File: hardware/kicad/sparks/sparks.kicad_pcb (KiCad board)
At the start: 2 copper layers, 39 parts, among them J1 Conn_02x04_Odd_Even, J2 TP4056 Breakout, SW1 SW_Push, U1 MAX7219, U2 ESP32-C3-SuperMini

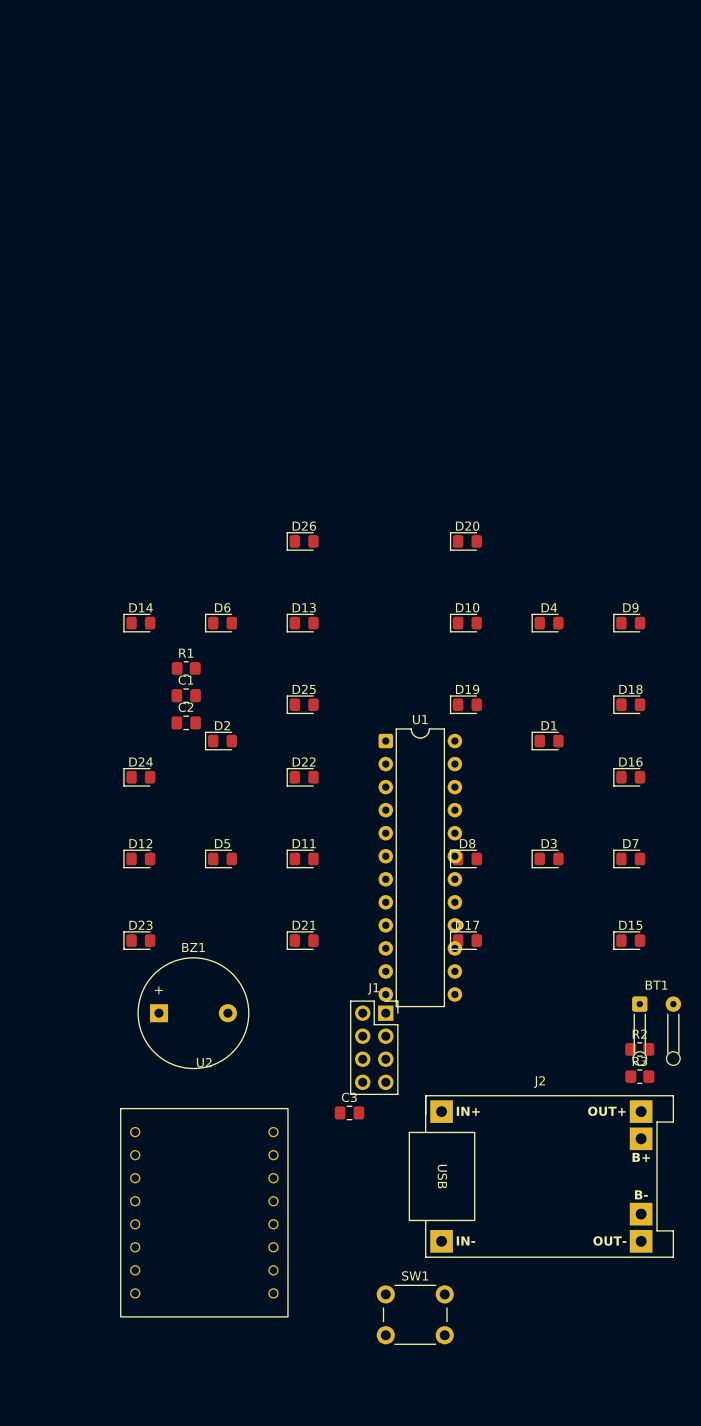
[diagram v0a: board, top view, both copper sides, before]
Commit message: Correct the panel to a 7x7 grid
The previous placement generated an extra empty column, because X
sat on an odd half-step while every other letter fell on a whole
one. The panel is a 7x7 grid with 26 of the 49 cells filled:

    O M T E I S H
    Q G - - U V -
    - Z - - F - -
    Y K N A R L -
    - C - - - - -
    - X D W P - -
    - - B J - - -

Row 0 is the repeated-symbol spine, reading H S I E outward to the
right and T M O to the left. Row 3 is the second spine, where the
code switches symbol once: A R L rightward, N K Y leftward.
Everything else hangs off those two rows, which is why the middle
rows are sparse.

The panel is now 48 x 42 mm with 7 mm between LEDs.

Move the CC1101 socket to the top edge so the antenna points away
from the user when the device is held, and reposition the rest of
the components around the smaller panel. Board outline is
66 x 106 mm.
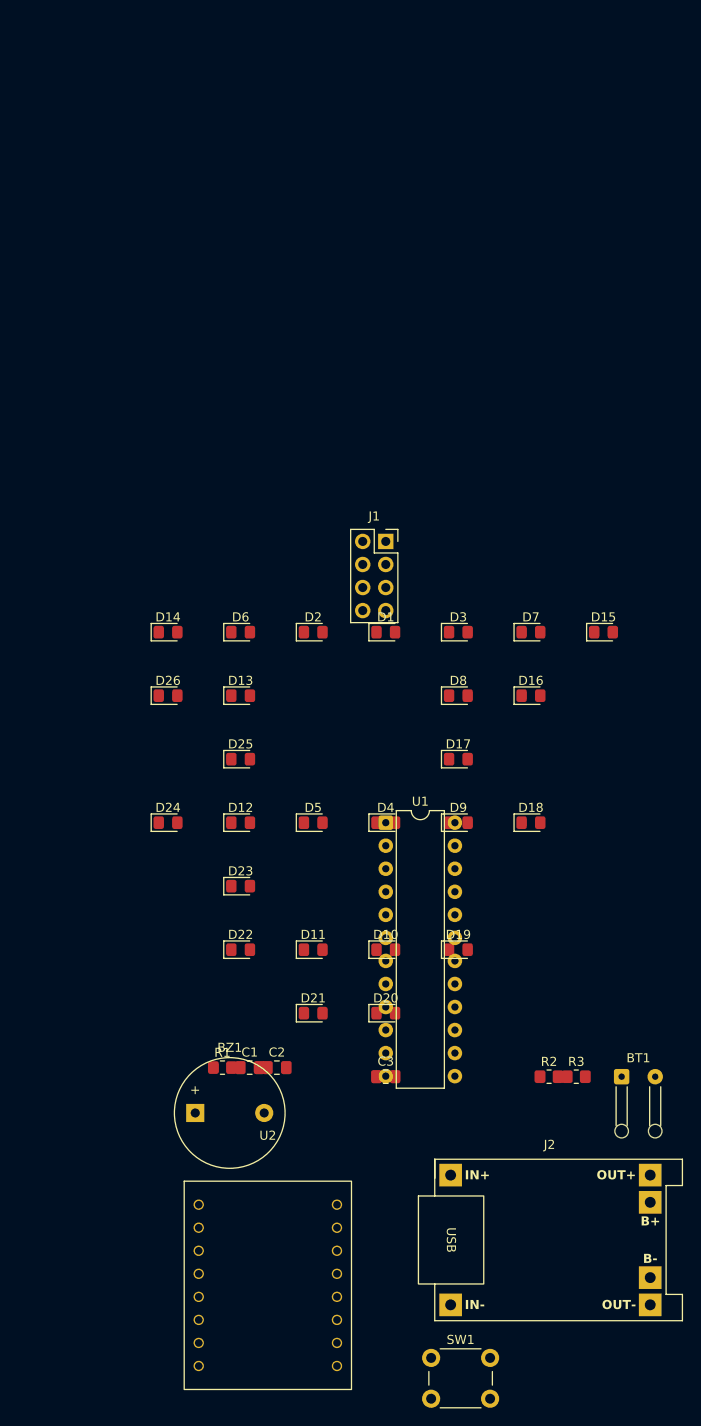
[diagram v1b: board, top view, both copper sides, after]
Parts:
- moved D20 52.8 mm to (150.0, 150.0)
- moved J1 52.0 mm to (150.0, 98.0)
- moved R1 44.2 mm to (132.0, 156.0)
- moved C1 41.6 mm to (135.0, 156.0)
- moved C2 39.3 mm to (138.0, 156.0)
- moved D10 37.1 mm to (150.0, 143.0)
- moved D15 34.1 mm to (174.0, 108.0)
- moved D9 29.1 mm to (158.0, 129.0)
- moved D4 28.4 mm to (150.0, 129.0)
- moved D7 27.3 mm to (166.0, 108.0)
- moved D19 27.0 mm to (158.0, 143.0)
- moved D3 26.9 mm to (158.0, 108.0)
- moved D26 22.7 mm to (126.0, 115.0)
- moved D1 21.6 mm to (150.0, 108.0)
- moved D22 20.2 mm to (134.0, 143.0)
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
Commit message: Mount the CC1101 socket at the board edge
The module plugs into the socket and overhangs the board entirely,
so the board carries only the 2x4 socket rather than the module's
full 28 mm length. The body and antenna extend past the top edge,
away from the user.

This keeps the board at 66 x 101 mm. Placing the module on the
board instead would have pushed it to 66 x 123 mm, since the
antenna exits the short edge opposite the pin header and the whole
module would have needed room above the panel.

Note in board_outline.txt that the module is held only by its eight
pins, so the case should brace it.
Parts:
- moved J1 2.00 mm to (150.0, 100.0)
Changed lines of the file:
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@@
 	(footprint "Connector_PinSocket_2.54mm:PinSocket_2x04_P2.54mm_Vertical"
 		(layer "F.Cu")
-		(at 150 98)
+		(at 150 100)
 		(descr "Through hole straight socket strip, 2x04, 2.54mm pitch, double rows (from Kicad 4.0.7), script generated")
 		(tags "Through hole socket strip THT 2x04 2.54mm double row")

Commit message: Rotate the CC1101 socket so the antenna points away from the user
PinSocket_2x04_P2.54mm_Vertical places 4 rows along Y and 2 columns
along X at rotation 0, not the other way round. With the socket
unrotated the module's length ran horizontally and the antenna
pointed out the side of the board.

Rotating the socket 90 degrees puts the four-pin row along X, so the
module's length runs vertically and the antenna extends past the top
edge, away from the user.
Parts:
- turned J1 to 90 degrees
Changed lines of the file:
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@@
 	(footprint "Connector_PinSocket_2.54mm:PinSocket_2x04_P2.54mm_Vertical"
 		(layer "F.Cu")
-		(at 150 100)
+		(at 150 100 90)
 		(descr "Through hole straight socket strip, 2x04, 2.54mm pitch, double rows (from Kicad 4.0.7), script generated")
 		(tags "Through hole socket strip THT 2x04 2.54mm double row")

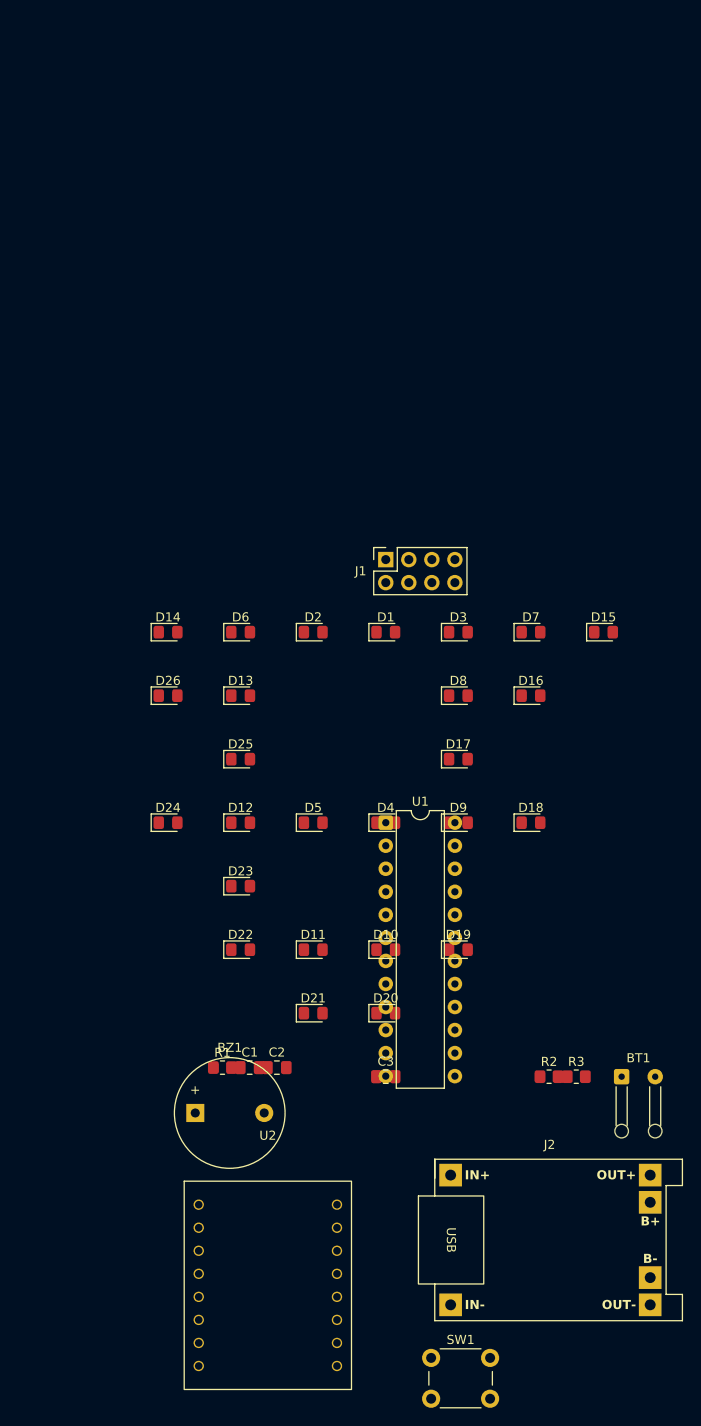
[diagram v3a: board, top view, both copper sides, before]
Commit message: Add a CC1101 socket footprint with the module's own pin numbering
The stock PinSocket_2x04 numbers pads 2/1, 4/3, 6/5, 8/7 across the
two rows, which put pin 1 on the outward-facing row. The module has
pin 1 (GND) on the row nearest the board and pin 2 (3V3) on the
outward row.

No rotation of the stock footprint produces that arrangement: 90 and
270 turn it sideways into two columns of four, and 180 swaps the
columns as well as the rows. It needs a mirror, which a footprint
cannot do without changing layers.

Add Sparks:CC1101_Socket_2x04 with pad positions written explicitly
so that at rotation 0 the top row is 2 4 6 8 and the bottom row,
against the board, is 1 3 5 7.

Register the Sparks.pretty library in fp-lib-table.
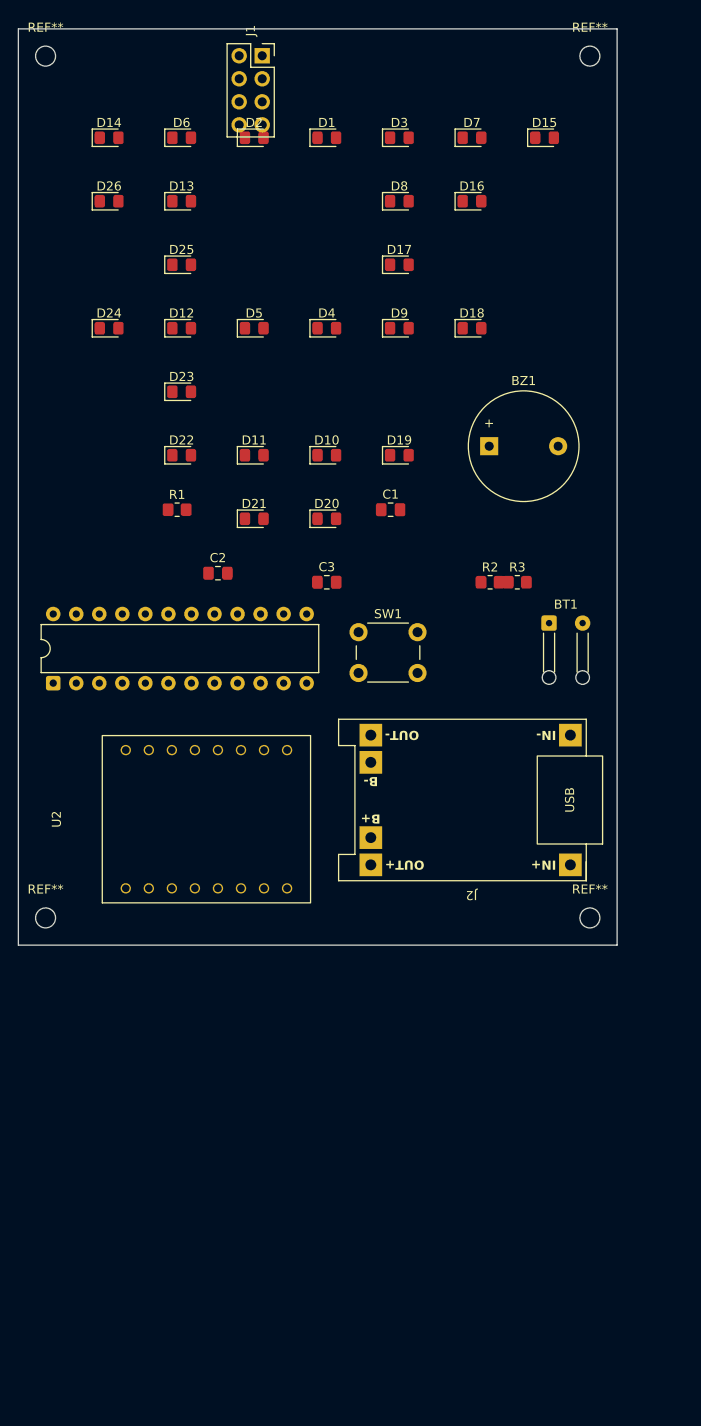
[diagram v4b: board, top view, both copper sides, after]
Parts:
- added REF**: MountingHole_2.2mm_M2, MountingHole:MountingHole_2.2mm_M2, F.Cu at (172.5, 44.5)
- added REF**: MountingHole_2.2mm_M2, MountingHole:MountingHole_2.2mm_M2, F.Cu at (112.5, 139.5)
- added REF**: MountingHole_2.2mm_M2, MountingHole:MountingHole_2.2mm_M2, F.Cu at (172.5, 139.5)
- added REF**: MountingHole_2.2mm_M2, MountingHole:MountingHole_2.2mm_M2, F.Cu at (112.5, 44.5)
- J1: footprint Connector_PinSocket_2.54mm:PinSocket_2x04_P2.54mm_Vertical -> Sparks:CC1101_Socket_2x04
- moved SW1 80.4 mm to (147.0, 108.0)
- moved BZ1 80.3 mm to (161.4, 87.5)
- moved C1 63.4 mm to (150.5, 94.5)
- moved R1 61.7 mm to (127.0, 94.5)
- moved J1 57.2 mm to (136.4, 44.5), turned to 0 degrees
- moved C2 54.9 mm to (131.5, 101.5)
- moved C3 54.9 mm to (143.5, 102.5)
- moved D1 54.9 mm to (143.5, 53.5)
- moved D10 54.9 mm to (143.5, 88.5)
- moved D11 54.9 mm to (135.5, 88.5)
- moved D12 54.9 mm to (127.5, 74.5)
- moved D13 54.9 mm to (127.5, 60.5)
- moved D14 54.9 mm to (119.5, 53.5)
- moved D15 54.9 mm to (167.5, 53.5)
- moved D16 54.9 mm to (159.5, 60.5)
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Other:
- board outline added: 66 x 101 mm
